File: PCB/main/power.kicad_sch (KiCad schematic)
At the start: 24 parts, among them Q1 AO3401A, Q2 Q_PMOS_DGS, U1 TP4056, U2 LM3940, U3 LM358, U8 AP2007

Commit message: Finished initial design
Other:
- company: UCT -> University of Cape Town
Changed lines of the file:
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@@
     (date "2022-03-11")
     (rev "V0.3")
-    (company "UCT")
-    (comment 1 "Author: WLSCAM007")
+    (company "University of Cape Town")
+    (comment 1 "@Author WLSCAM007")
+    (comment 2 "@Project EEE3088F-Team-9")
   )
   (junction (at 55.88 168.91) (diameter 0) (color 0 0 0 0)

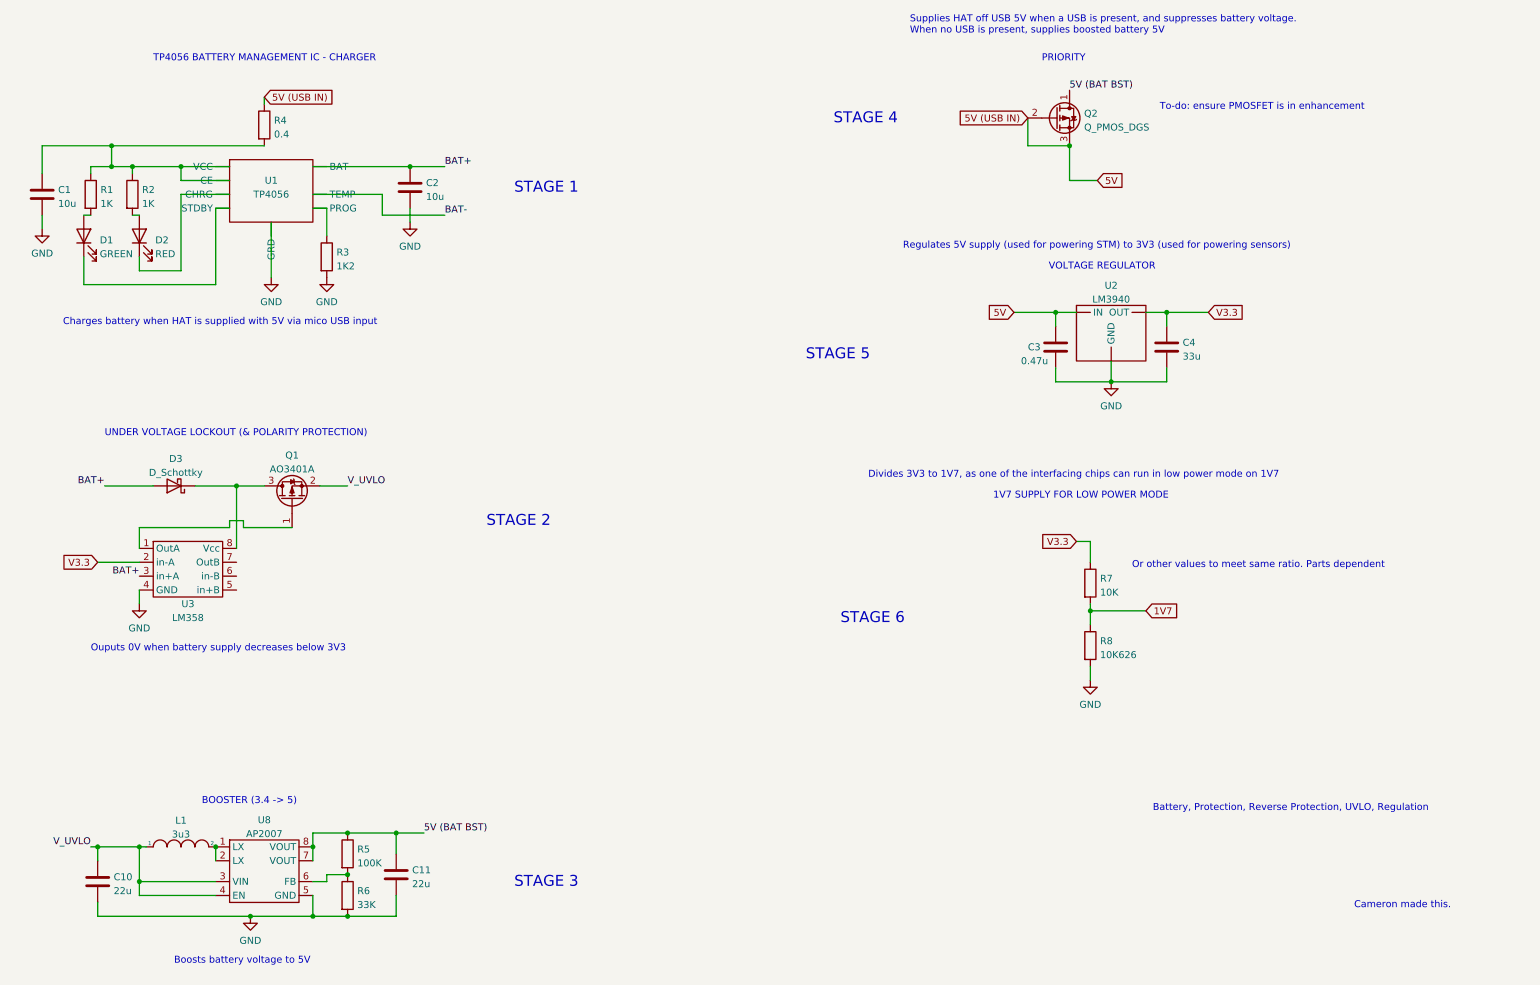
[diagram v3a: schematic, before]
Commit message: Fiddled a bit with labels
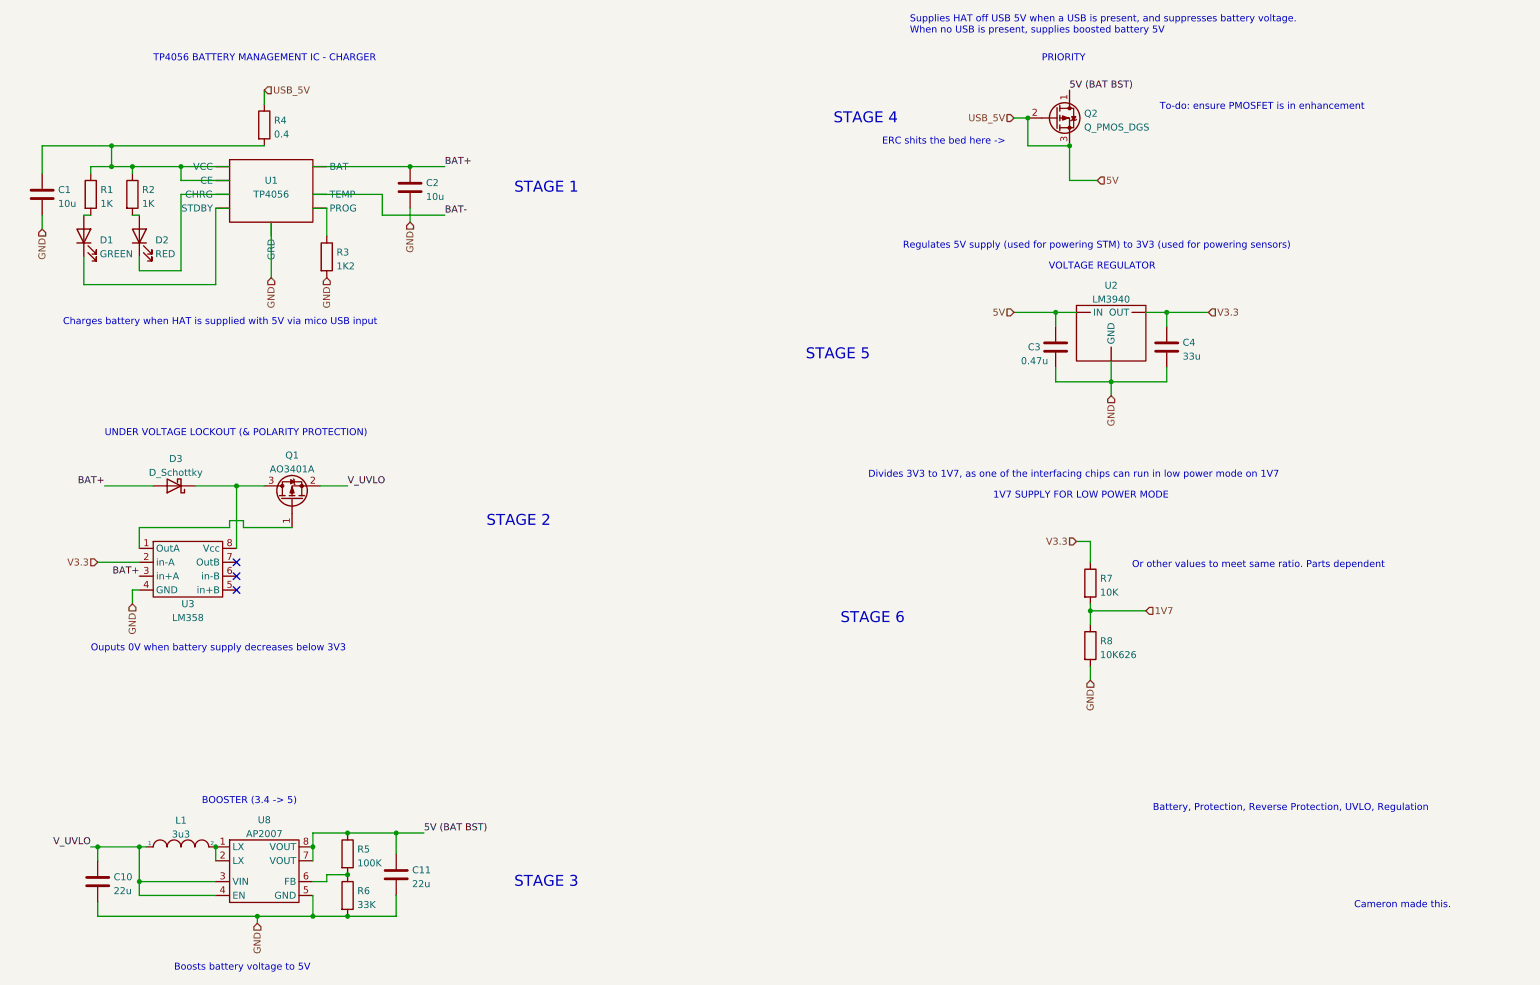
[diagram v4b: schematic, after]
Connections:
- no-connect marks 0 -> 3
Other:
- note added: "ERC shits the bed here ->"

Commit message: Added Footprint and symbol files
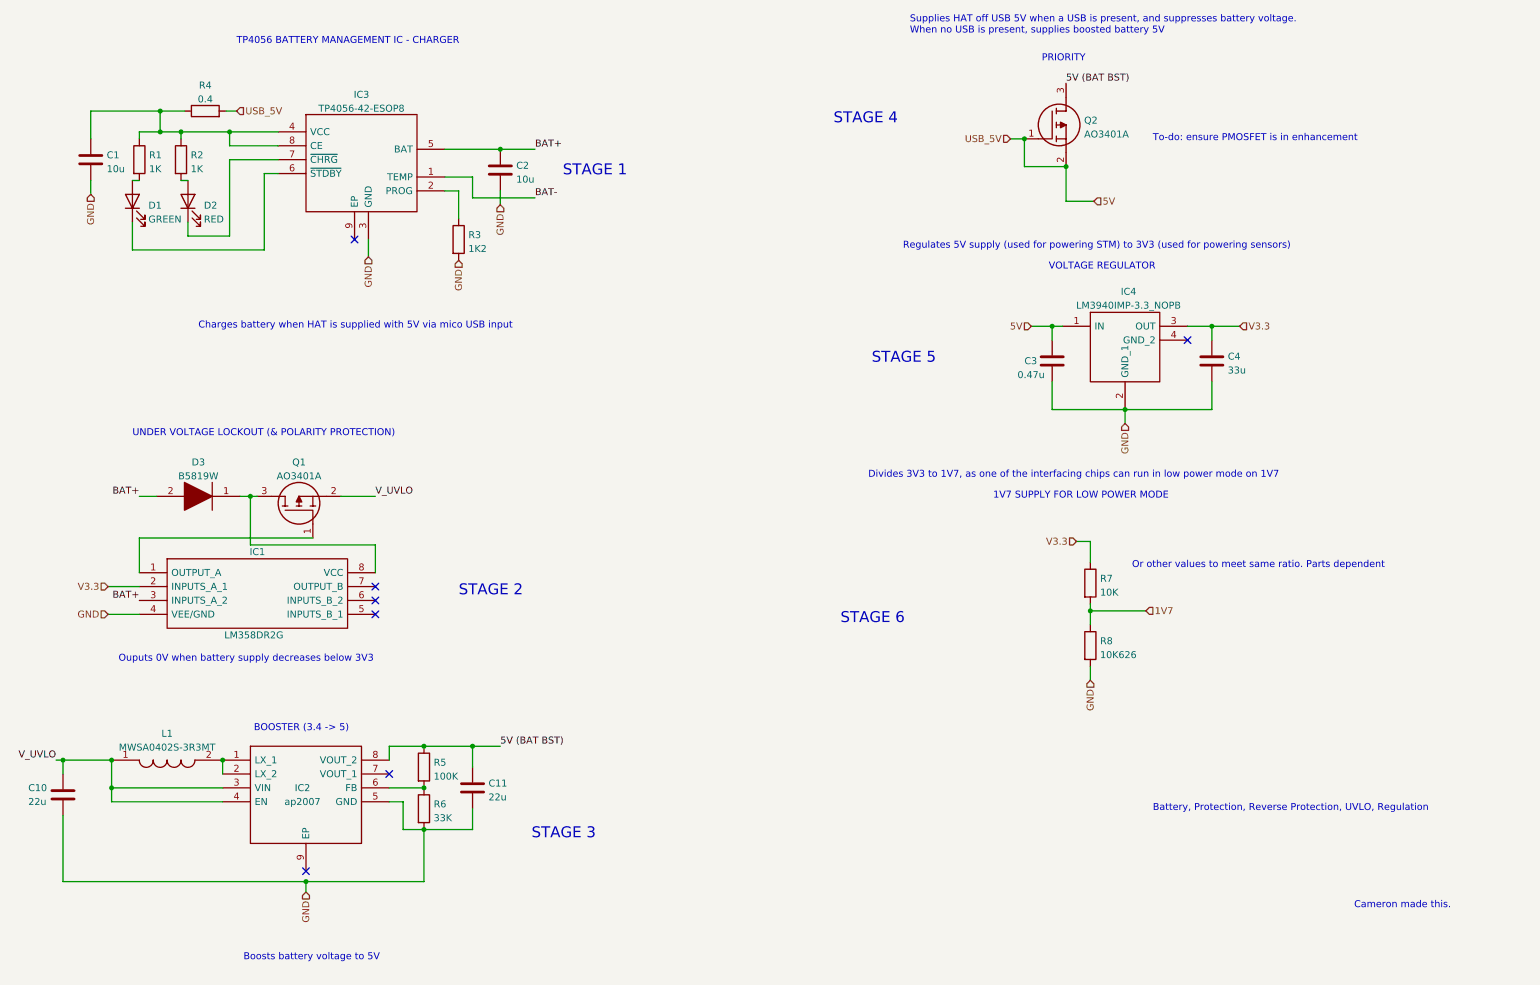
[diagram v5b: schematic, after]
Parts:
- removed D3: D_Schottky, symbol Device:D_Schottky
- removed L1: 3u3, symbol pspice:INDUCTOR
- removed Q1: AO3401A, Package_TO_SOT_SMD:SOT-23, symbol Transistor_FET:AO3401A
- removed Q2: Q_PMOS_DGS, symbol Device:Q_PMOS_DGS
- removed U1: TP4056, symbol 000_MY_SYMBOLS:TP4056
- removed U2: LM3940, symbol 000_MY_SYMBOLS:LM3940
- removed U3: LM358, symbol 000_MY_SYMBOLS:LM358
- removed U8: AP2007, symbol 000_MY_SYMBOLS:AP2007
- added D3: B5819W, symbol B5819W:B5819W
- added IC1: LM358DR2G, symbol LM358DR2G:LM358DR2G
- added IC2: ap2007, symbol ap2007:ap2007
- added IC3: TP4056-42-ESOP8, symbol TP4056-42-ESOP8:TP4056-42-ESOP8
- added IC4: LM3940IMP-3.3_NOPB, symbol LM3940IMP-3.3_NOPB:LM3940IMP-3.3_NOPB
- added L1: MWSA0402S-3R3MT, symbol MWSA0402S-3R3MT:MWSA0402S-3R3MT
- added Q1, Q2: AO3401A, symbol AO3401A:AO3401A
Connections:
- net 5V: now also R4.2, IC4.1 (IN), Q2.1, Q2.2; no longer R4.1
- net 5V (BAT BST): now also IC2.8 (VOUT_2), Q2.3
- net BAT+: now also D3.2, IC1.3 (INPUTS_A_2), IC3.5 (BAT)
- net BAT-: now also IC3.1 (TEMP)
- net GND: now also IC1.4 (VEE/GND), IC2.5 (GND), IC3.3 (GND), IC4.2 (GND_1)
- net V3.3: now also IC1.2 (INPUTS_A_1), IC4.3 (OUT)
- net V_UVLO: now also IC2.3 (VIN), IC2.4 (EN), L1.1, Q1.2
- net at D1.1 (K): now also IC3.6 (~{STDBY})
- net at D2.1 (K): now also IC3.7 (~{CHRG})
- net at C1.1, R1.1, R2.1: now also R4.1, IC3.4 (VCC), IC3.8 (CE); no longer R4.2
- net at R3.1: now also IC3.2 (PROG)
- net at R5.2, R6.1: now also IC2.6 (FB)
- new net: IC2.1 (LX_1), IC2.2 (LX_2), L1.2
- new net: IC1.1 (OUTPUT_A), Q1.1
- new net: D3.1, IC1.8 (VCC), Q1.3
- no-connect marks 3 -> 7
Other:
- note removed: "ERC shits the bed here ->"
- moved on the sheet: C1, C10, C11, C2, C3, C4, D1, D2, R1, R2, R3, R4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

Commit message: Annotated power schem, HAVE NOT ADDED INDUCTOR. v0.4
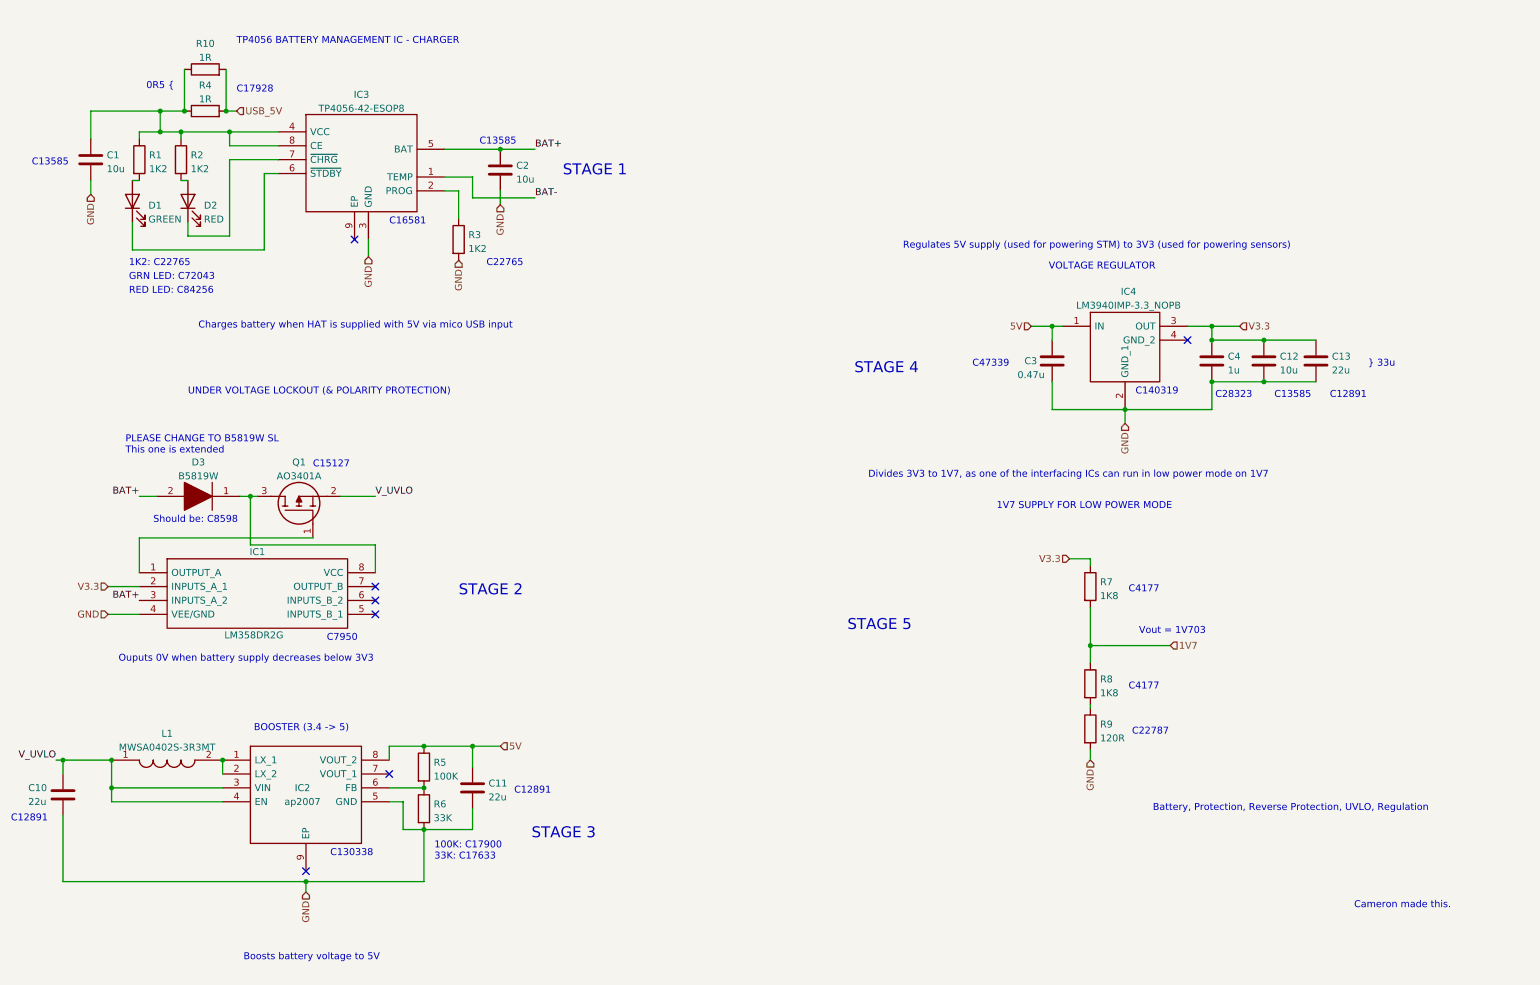
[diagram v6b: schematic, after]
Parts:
- removed Q2: AO3401A, symbol AO3401A:AO3401A
- added C12: 10u, symbol Device:C
- added C13: 22u, symbol Device:C
- added R10: 1R, symbol Device:R
- added R9: 120R, symbol Device:R
- C4: value 33u -> 1u
- R1, R2: value 1K -> 1K2
- R4: value 0.4 -> 1R
- R7: value 10K -> 1K8
- R8: value 10K626 -> 1K8
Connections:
- net 5V (BAT BST) is gone; now on net 5V: C11.1, IC2.8 (VOUT_2), R5.1
- net 5V: no longer R4.2
- net GND: now also C12.2, C13.2, R9.2; no longer R8.2
- net V3.3: now also C12.1, C13.1
- net at C1.1, IC3.4 (VCC), IC3.8 (CE)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: now also R10.1
- new net: R8.2, R9.1
- new net USB_5V: R10.2, R4.2
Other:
- note added: "0R5 {"
- note added: "100K: C17900 33K: C17633"
- note added: "1K2: C22765"
- note added: "C12891"
- note added: "C130338"
- note added: "C13585"
- note added: "C140319"
- note added: "C15127"
- note added: "C16581"
- note added: "C17928"
- note added: "C22765"
- note added: "C22787"
- note added: "C28323"
- note added: "C4177"
- note added: "C47339"
- note added: "C7950"
- note added: "Divides 3V3 to 1V7, as one of the interfacing ICs can run in low power mode on 1V7"
- note added: "GRN LED: C72043"
- note added: "PLEASE CHANGE TO B5819W SL This one is extended"
- note added: "RED LED: C84256"
- note added: "Should be: C8598"
- note added: "Vout = 1V703"
- note added: "} 33u"
- note removed: "Divides 3V3 to 1V7, as one of the interfacing chips can run in low power mode on 1V7"
- note removed: "Or other values to meet same ratio. Parts dependent"
- note removed: "PRIORITY"
- note removed: "STAGE 6"
- note removed: "Supplies HAT off USB 5V when a USB is present, and suppresses battery voltage. When no USB is present, supplies boosted battery 5V"
- note removed: "To-do: ensure PMOSFET is in enhancement"
- moved on the sheet: R7

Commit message: Fixed orientation of MOSFET in UVLO. Did not add power switch due to budget. Annotated UVLO inductor. v0.4
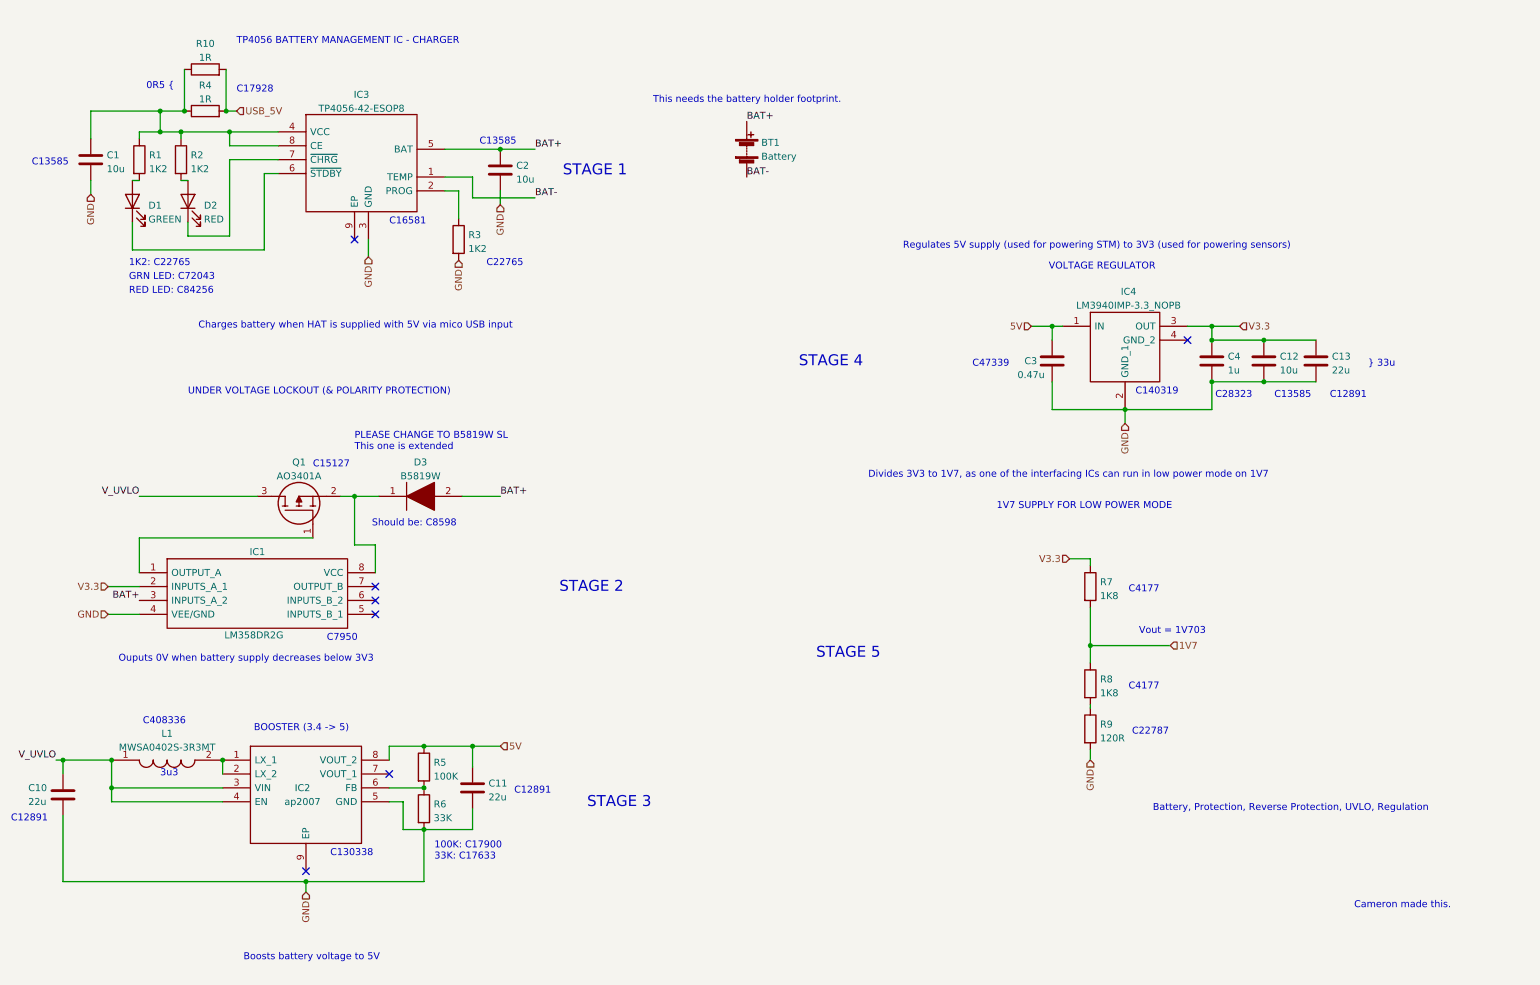
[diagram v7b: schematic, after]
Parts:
- added BT1: Battery, symbol Device:Battery
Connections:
- net BAT+: now also BT1.1 (+)
- net BAT-: now also BT1.2 (-)
- net V_UVLO: now also Q1.3; no longer Q1.2
- net at D3.1, IC1.8 (VCC): now also Q1.2; no longer Q1.3
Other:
- note added: "3u3"
- note added: "C408336"
- note added: "This needs the battery holder footprint."
